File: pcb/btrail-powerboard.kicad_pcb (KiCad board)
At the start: 2 copper layers, 44.5 x 52.8 mm, 13 parts, among them J1 RJ45_Shielded, Q1 IRLZ34N, Q2 IRLZ34N

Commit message: Sync for coop purposes
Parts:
- Vin DC-DC: renamed from Vin_DC-DC1
- renumbered 5V+1 to +5V
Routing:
- net +24V: track 132.6 -> 135.9 mm
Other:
- outline, holes or cut-outs redrawn

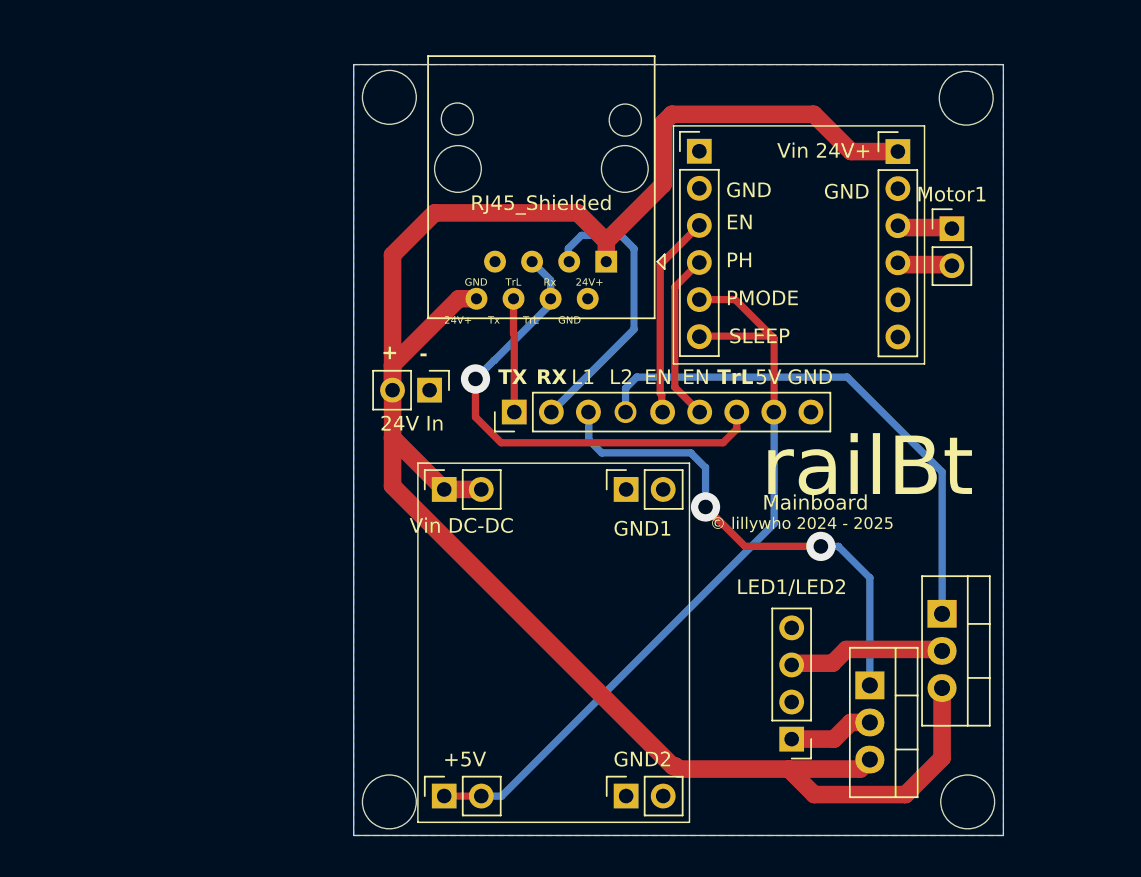
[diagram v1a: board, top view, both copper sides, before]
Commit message: New board revision: Add full wave rectifier
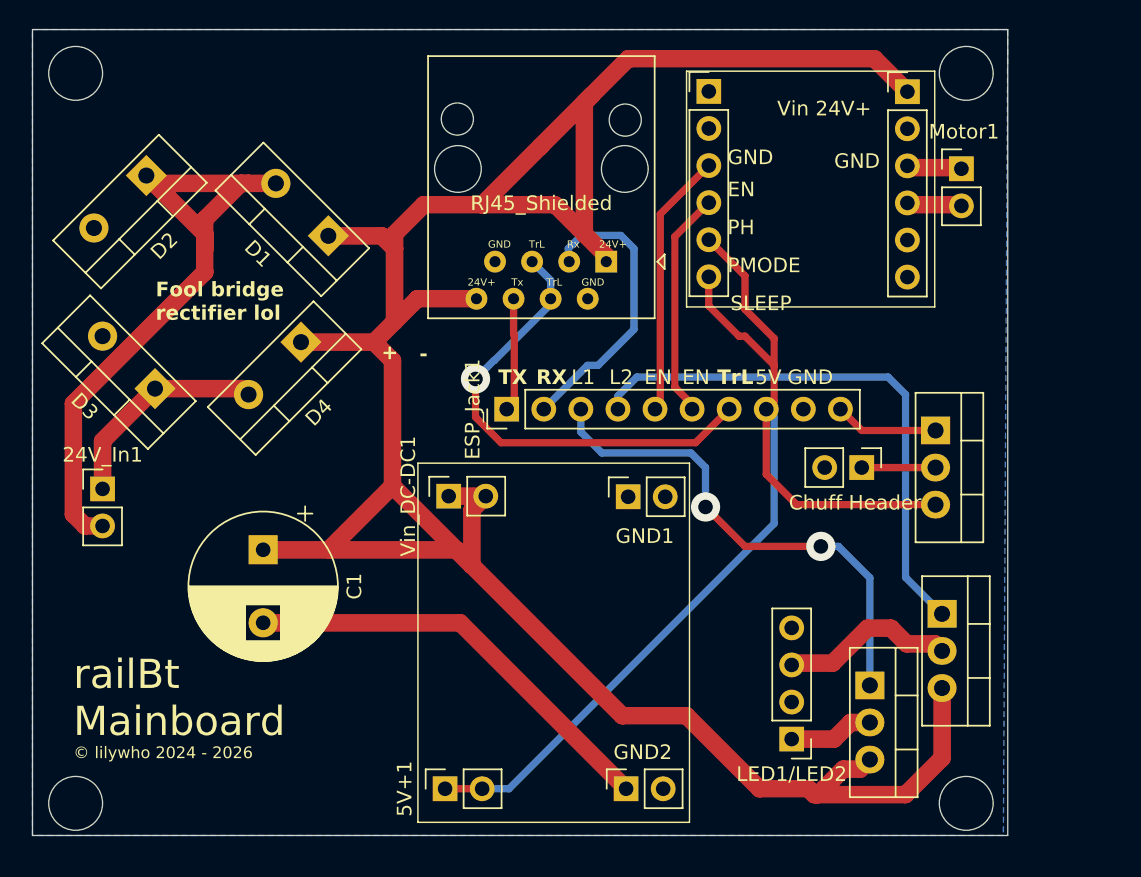
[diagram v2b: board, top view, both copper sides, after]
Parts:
- removed +5V: Conn_01x02, Connector_PinSocket_2.54mm:PinSocket_1x02_P2.54mm_Vertical
- removed 24V In: Conn_01x02_Pin, Connector_PinHeader_2.54mm:PinHeader_1x02_P2.54mm_Vertical
- removed ESP32_jack1: Conn_01x09_Pin, Connector_PinHeader_2.54mm:PinHeader_1x09_P2.54mm_Vertical
- removed Vin DC-DC: Conn_01x01, Connector_PinSocket_2.54mm:PinSocket_1x02_P2.54mm_Vertical
- added 24V_In1: Conn_01x02_Pin, Connector_PinHeader_2.54mm:PinHeader_1x02_P2.54mm_Vertical, F.Cu at (173.0, 47.5)
- added 5V+1: Conn_01x02, Connector_PinSocket_2.54mm:PinSocket_1x02_P2.54mm_Vertical, F.Cu at (196.5, 68.0)
- added C1: 470uF_35V, Capacitor_THT:CP_Radial_D10.0mm_P5.00mm, F.Cu at (184.0, 51.6)
- added Chuff_Jack1: Conn_01x02_Pin, Connector_PinHeader_2.54mm:PinHeader_1x02_P2.54mm_Vertical, F.Cu at (225.0, 46.0)
- added D1: MBR735, Package_TO_SOT_THT:TO-220-2_Vertical, F.Cu at (188.5, 30.1)
- added D2: MBR735, Package_TO_SOT_THT:TO-220-2_Vertical, F.Cu at (176.0, 26.0)
- added D3: MBR735, Package_TO_SOT_THT:TO-220-2_Vertical, F.Cu at (176.6, 40.6)
- added D4: MBR735, Package_TO_SOT_THT:TO-220-2_Vertical, F.Cu at (186.6, 37.4)
- added ESP_Jack1: Conn_01x10_Pin, Connector_PinHeader_2.54mm:PinHeader_1x10_P2.54mm_Vertical, F.Cu at (200.7, 42.0)
- added Q3: IRL540NPBF, Package_TO_SOT_THT:TO-220-3_Vertical, F.Cu at (230.1, 43.5)
- added Vin_DC-DC1: Conn_01x01, Connector_PinSocket_2.54mm:PinSocket_1x02_P2.54mm_Vertical, F.Cu at (196.7, 48.0)
- Q1, Q2: value IRLZ34N -> IRL540NPBF
- moved DRV8874_left1 4.15 mm to (214.5, 20.2)
- moved DRV8874_right1 4.15 mm to (228.1, 20.3)
- moved Motor1 4.15 mm to (231.8, 25.5)
- moved GND1 0.52 mm to (209.0, 48.0)
- moved GND2 0.50 mm to (208.9, 68.0)
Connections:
- net +24V renamed /24VDC+
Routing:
- net /AC_IN1: track 0.00 -> 46.0 mm
- net /24VDC+: track 135.9 -> 181.2 mm
- net GND: track 0.00 -> 29.6 mm
- net +5V: track 54.2 -> 76.9 mm
- net /AC_IN2: track 0.00 -> 14.9 mm
- net Net-(ESP_Jack1-Pin_10): track 0.00 -> 7.12 mm
- net Net-(Chuff_Jack1-Pin_1): track 0.00 -> 5.06 mm
- net Net-(DRV8874_left1-Pin_3): track 13.9 -> 17.7 mm
- net Net-(DRV8874_left1-Pin_4): track 11.6 -> 15.3 mm
- net Net-(ESP_Jack1-Pin_4): track 36.0 -> 37.7 mm
- net Net-(ESP_Jack1-Pin_7): track 33.5 -> 32.0 mm
- net Net-(LED1/LED2-Pin_3): track 10.8 -> 11.7 mm
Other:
- board size 44.5 x 52.8 mm -> 66.8 x 55.2 mm
- board text added: "Chuff Header"
- board text added: "Fool bridge rectifier lol"
- board text added: "boom"
- board text added: "railBt Mainboard"
- board text added: "© lilywho 2024 - 2026"
- board text removed: "Mainboard"
- board text removed: "railBt"
- board text removed: "© lillywho 2024 - 2025"

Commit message: Update PCB to latest full bridge rectifier version
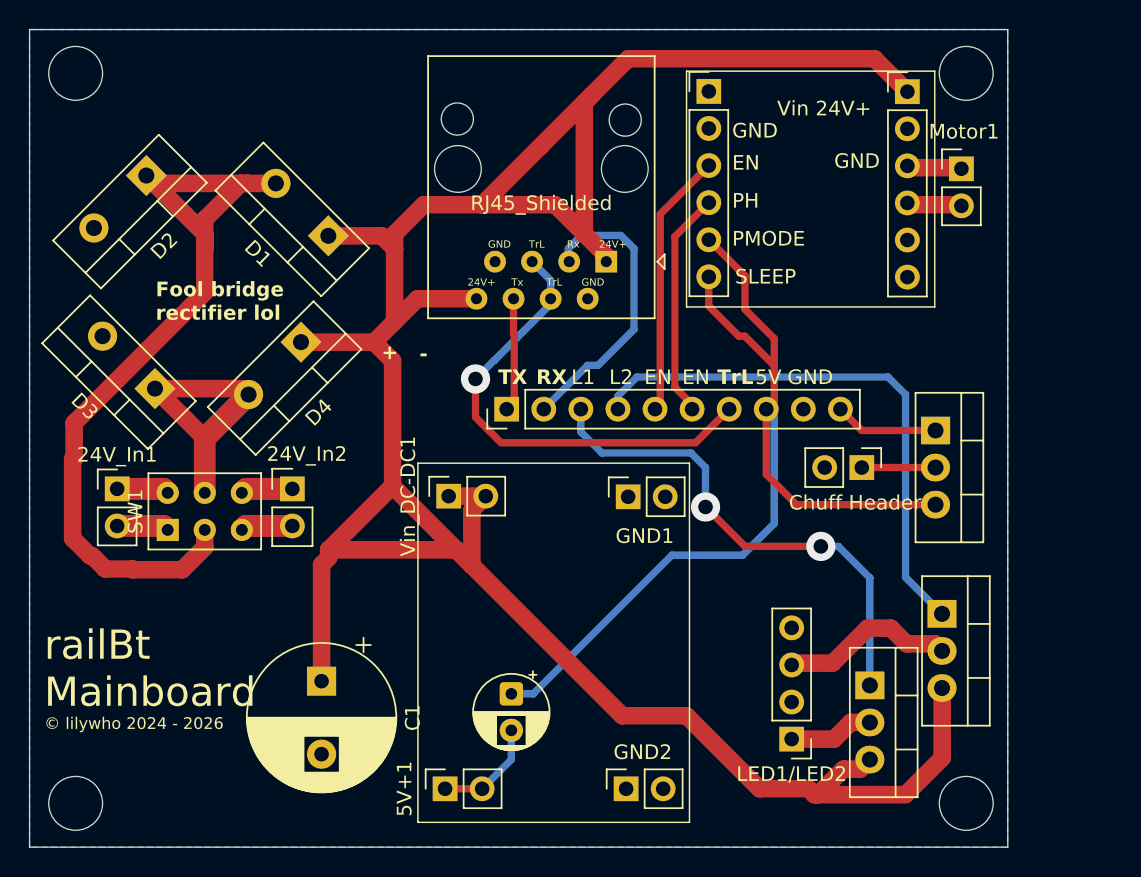
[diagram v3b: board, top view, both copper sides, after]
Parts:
- added 24V_In2: Conn_01x02_Pin, Connector_PinHeader_2.54mm:PinHeader_1x02_P2.54mm_Vertical, F.Cu at (186.0, 47.5)
- added C2: Capacitor_PO, Capacitor_THT:CP_Radial_D5.0mm_P2.50mm, F.Cu at (201.0, 61.5)
- added SW1: SW_Slide_DPDT, Button_Switch_THT:SW_NKK_G1xJP, F.Cu at (177.5, 50.3)
- moved C1 9.85 mm to (188.0, 60.6)
- moved 24V_In1 1.00 mm to (174.0, 47.5)
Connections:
- net /24VDC+ renamed +24V
- 24V_In1 pad 1: /AC_IN2 -> /TRK_IN2
- 24V_In1 pad 2: /AC_IN1 -> /TRK_IN1
- D1 pad 2: /AC_IN1 -> /IN1
- D2 pad 1: /AC_IN1 -> /IN1
- D3 pad 1: /AC_IN2 -> /IN2
- D4 pad 2: /AC_IN2 -> /IN2
- DRV8874_left1 pad 5: +5V -> Net-(DRV8874_left1-Pin_5)
- DRV8874_left1 pad 6: +5V -> Net-(DRV8874_left1-Pin_5)
- ESP_Jack1 pad 8: +5V -> Net-(DRV8874_left1-Pin_5)
- Q3 pad 3: +5V -> Net-(DRV8874_left1-Pin_5)
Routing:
- net Net-(DRV8874_left1-Pin_5): track 0.00 -> 69.7 mm
- net +5V: track 76.9 -> 7.37 mm
- net /IN1: track 0.00 -> 57.2 mm
- net /AC_IN1: track 46.0 -> 0.00 mm
- net GND: track 29.6 -> 0.00 mm
- net /IN2: track 0.00 -> 19.4 mm
- net /AC_IN2: track 14.9 -> 0.00 mm
- net +24V: track 181.2 -> 186.0 mm
- net /BAT_IN1: track 0.00 -> 3.57 mm
- net /TRK_IN1: track 0.00 -> 3.57 mm
- net /TRK_IN2: track 0.00 -> 3.57 mm
- net /BAT_IN2: track 0.00 -> 3.57 mm
- net Net-(ESP_Jack1-Pin_1): track 7.80 -> 7.06 mm
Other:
- board size 66.8 x 55.2 mm -> 67 x 56 mm
